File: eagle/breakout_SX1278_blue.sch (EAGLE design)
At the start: 19 parts, among them X1 734120110

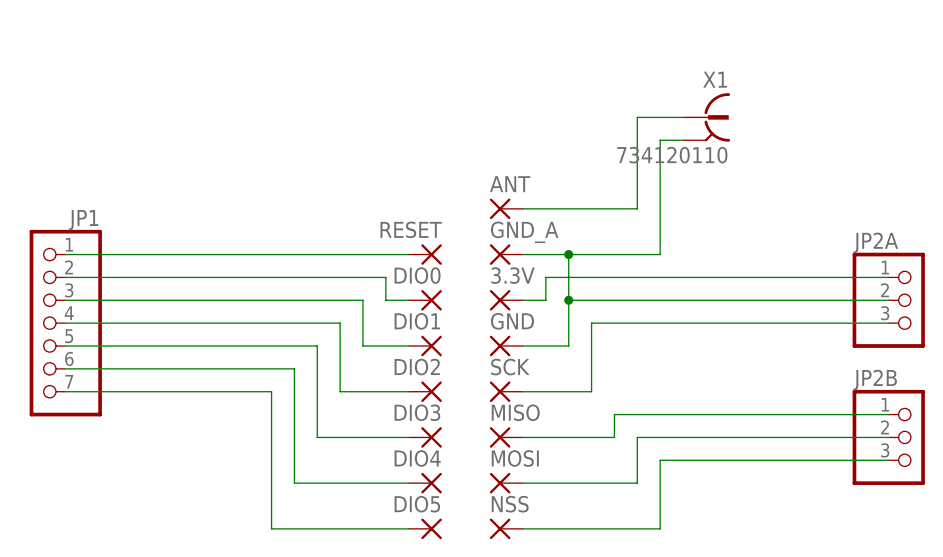
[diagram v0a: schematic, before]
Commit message: Module layout update
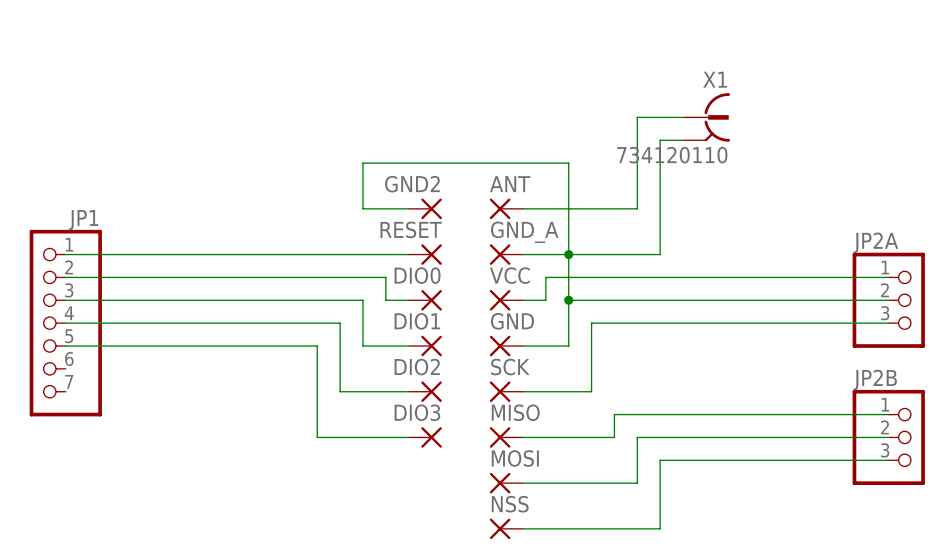
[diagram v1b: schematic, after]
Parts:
- removed DIO4, DIO5: (no value), wirepad:SMD1
- added GND2: (no value), wirepad:SMD1
- renumbered 3.3V to VCC
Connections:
- removed net DIO4: DIO4.P, JP1.6
- removed net DIO5: DIO5.P, JP1.7
- net GND: now also GND2.P
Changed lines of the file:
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@@
 <?xml version="1.0" encoding="utf-8"?>
 <!DOCTYPE eagle SYSTEM "eagle.dtd">
-<eagle version="8.0.2">
+<eagle version="8.1.0">
 <drawing>
 <settings>
@@
 <part name="DIO2" library="wirepad" deviceset="SMD1" device=""/>
 <part name="DIO3" library="wirepad" deviceset="SMD1" device=""/>
-<part name="DIO4" library="wirepad" deviceset="SMD1" device=""/>
-<part name="DIO5" library="wirepad" deviceset="SMD1" device=""/>
 <part name="GND_A" library="wirepad" deviceset="SMD1" device=""/>
 <part name="ANT" library="wirepad" deviceset="SMD1" device=""/>
-<part name="3.3V" library="wirepad" deviceset="SMD1" device=""/>
+<part name="VCC" library="wirepad" deviceset="SMD1" device=""/>
 <part name="GND" library="wirepad" deviceset="SMD1" device=""/>
 <part name="SCK" library="wirepad" deviceset="SMD1" device=""/>
@@
 <part name="JP2A" library="pinhead" deviceset="PINHD-1X3" device=""/>
 <part name="JP2B" library="pinhead" deviceset="PINHD-1X3" device=""/>
+<part name="GND2" library="wirepad" deviceset="SMD1" device=""/>
 </parts>
 <sheets>
@@
 <instance part="DIO2" gate="1" x="60.96" y="45.72" rot="MR0"/>
 <instance part="DIO3" gate="1" x="60.96" y="40.64" rot="MR0"/>
-<instance part="DIO4" gate="1" x="60.96" y="35.56" rot="MR0"/>
-<instance part="DIO5" gate="1" x="60.96" y="30.48" rot="MR0"/>
 <instance part="GND_A" gate="1" x="68.58" y="60.96"/>
 <instance part="ANT" gate="1" x="68.58" y="66.04"/>
-<instance part="3.3V" gate="1" x="68.58" y="55.88"/>
+<instance part="VCC" gate="1" x="68.58" y="55.88"/>
 <instance part="GND" gate="1" x="68.58" y="50.8"/>
 <instance part="SCK" gate="1" x="68.58" y="45.72"/>
@@
 <instance part="JP2A" gate="A" x="114.3" y="55.88"/>
 <instance part="JP2B" gate="A" x="114.3" y="40.64"/>
+<instance part="GND2" gate="1" x="60.96" y="66.04" rot="MR0"/>
 </instances>
 <busses>
@@
 </segment>
 </net>
-<net name="DIO4" class="0">
-<segment>
-<wire x1="58.42" y1="35.56" x2="45.72" y2="35.56" width="0.1524" layer="91"/>
-<wire x1="45.72" y1="35.56" x2="45.72" y2="48.26" width="0.1524" layer="91"/>
-<pinref part="JP1" gate="A" pin="6"/>
-<wire x1="45.72" y1="48.26" x2="20.32" y2="48.26" width="0.1524" layer="91"/>
-<pinref part="DIO4" gate="1" pin="P"/>
-</segment>
-</net>
-<net name="DIO5" class="0">
-<segment>
-<wire x1="58.42" y1="30.48" x2="43.18" y2="30.48" width="0.1524" layer="91"/>
-<wire x1="43.18" y1="30.48" x2="43.18" y2="45.72" width="0.1524" layer="91"/>
-<pinref part="JP1" gate="A" pin="7"/>
-<wire x1="43.18" y1="45.72" x2="20.32" y2="45.72" width="0.1524" layer="91"/>
-<pinref part="DIO5" gate="1" pin="P"/>
-</segment>
-</net>
 <net name="3.3V" class="0">
 <segment>
 <wire x1="71.12" y1="55.88" x2="73.66" y2="55.88" width="0.1524" layer="91"/>
 <wire x1="73.66" y1="55.88" x2="73.66" y2="58.42" width="0.1524" layer="91"/>
-<pinref part="3.3V" gate="1" pin="P"/>
+<pinref part="VCC" gate="1" pin="P"/>
 <wire x1="73.66" y1="58.42" x2="111.76" y2="58.42" width="0.1524" layer="91"/>
 <pinref part="JP2A" gate="A" pin="1"/>
@@
 <junction x="76.2" y="60.96"/>
 <pinref part="JP2A" gate="A" pin="2"/>
-</segment>
-</net>
+<pinref part="GND2" gate="1" pin="P"/>
+<wire x1="58.42" y1="66.04" x2="53.34" y2="66.04" width="0.1524" layer="91"/>
+<wire x1="53.34" y1="66.04" x2="53.34" y2="71.12" width="0.1524" layer="91"/>
+<wire x1="53.34" y1="71.12" x2="76.2" y2="71.12" width="0.1524" layer="91"/>
+<wire x1="76.2" y1="71.12" x2="76.2" y2="60.96" width="0.1524" layer="91"/>
+</segment>
+</net>

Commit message: Major layout update, read details
The layouts of shield and all breakout boards were changed to match the new multiprotocol standard.
IMPORTANT: The new shield is NOT compatible with the old breakout boards!
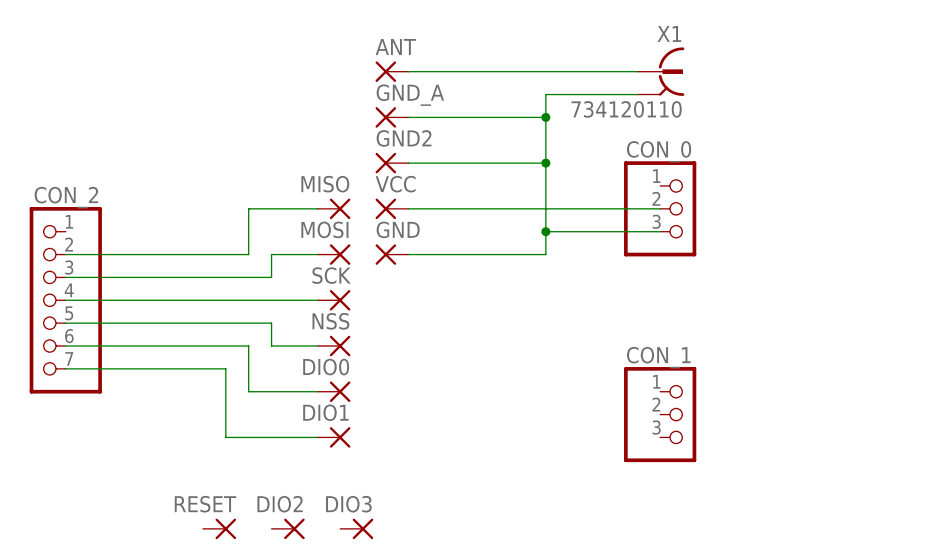
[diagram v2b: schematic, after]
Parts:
- removed JP1: (no value), pinhead:PINHD-1X7
- removed JP2A, JP2B: (no value), pinhead:PINHD-1X3
- added CON_0, CON_1: (no value), pinhead:PINHD-1X3
- added CON_2: (no value), pinhead:PINHD-1X7
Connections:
- removed net 3.3V: JP2A.1, VCC.P
- removed net DIO2: DIO2.P, JP1.4
- removed net DIO3: DIO3.P, JP1.5
- removed net RESET: JP1.1, RESET.P
- new net VCC: CON_0.2, VCC.P
- net DIO0: now also CON_2.6; no longer JP1.2
- net DIO1: now also CON_2.7; no longer JP1.3
- net GND: now also CON_0.3; no longer JP2A.2
- net MISO: now also CON_2.2; no longer JP2B.1
- net MOSI: now also CON_2.3; no longer JP2B.2
- net NSS: now also CON_2.5; no longer JP2B.3
- net SCK: now also CON_2.4; no longer JP2A.3
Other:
- moved on the sheet: ANT, DIO0, DIO1, DIO2, DIO3, GND, GND2, GND_A, MISO, MOSI, NSS, RESET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

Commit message: Release 1.0
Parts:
- renumbered VCC to 3.3V
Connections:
- net VCC renamed 3.3V
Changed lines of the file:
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@@
 <setting verticaltext="up"/>
 </settings>
-<grid distance="0.1" unitdist="inch" unit="inch" style="lines" multiple="1" display="yes" altdistance="0.01" altunitdist="inch" altunit="inch"/>
+<grid distance="0.1" unitdist="inch" unit="inch" style="lines" multiple="1" display="no" altdistance="0.01" altunitdist="inch" altunit="inch"/>
 <layers>
 <layer number="1" name="Top" color="4" fill="1" visible="no" active="no"/>
@@
 <part name="GND_A" library="wirepad" deviceset="SMD1" device=""/>
 <part name="ANT" library="wirepad" deviceset="SMD1" device=""/>
-<part name="VCC" library="wirepad" deviceset="SMD1" device=""/>
+<part name="3.3V" library="wirepad" deviceset="SMD1" device=""/>
 <part name="GND" library="wirepad" deviceset="SMD1" device=""/>
 <part name="SCK" library="wirepad" deviceset="SMD1" device=""/>
@@
 <instance part="GND_A" gate="1" x="55.88" y="76.2"/>
 <instance part="ANT" gate="1" x="55.88" y="81.28"/>
-<instance part="VCC" gate="1" x="55.88" y="66.04"/>
+<instance part="3.3V" gate="1" x="55.88" y="66.04"/>
 <instance part="GND" gate="1" x="55.88" y="60.96"/>
 <instance part="SCK" gate="1" x="50.8" y="55.88" rot="MR0"/>
@@
 </segment>
 </net>
-<net name="VCC" class="0">
+<net name="3.3V" class="0">
 <segment>
-<pinref part="VCC" gate="1" pin="P"/>
+<pinref part="3.3V" gate="1" pin="P"/>
 <pinref part="CON_0" gate="A" pin="2"/>
 <wire x1="58.42" y1="66.04" x2="86.36" y2="66.04" width="0.1524" layer="91"/>
